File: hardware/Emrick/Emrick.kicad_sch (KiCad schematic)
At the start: 86 parts, among them J1 LED_STRIP_CONNECTOR, J3 Conn_02x05_Odd_Even, J4 BATT_CONN, P1 USB_C_Plug_USB2.0, Q1 Q_NMOS_GSD, Q2 Q_NMOS_GSD, Q3 Q_NMOS_GSD, SW1 SW_SPST, U1 74HCT541, U2 CC1310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

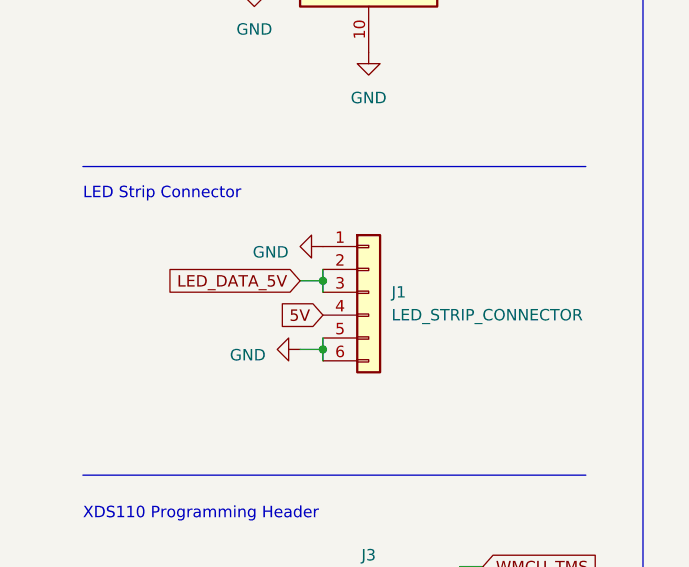
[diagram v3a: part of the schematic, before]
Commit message: update bom and change to horizontal PA connector footprint
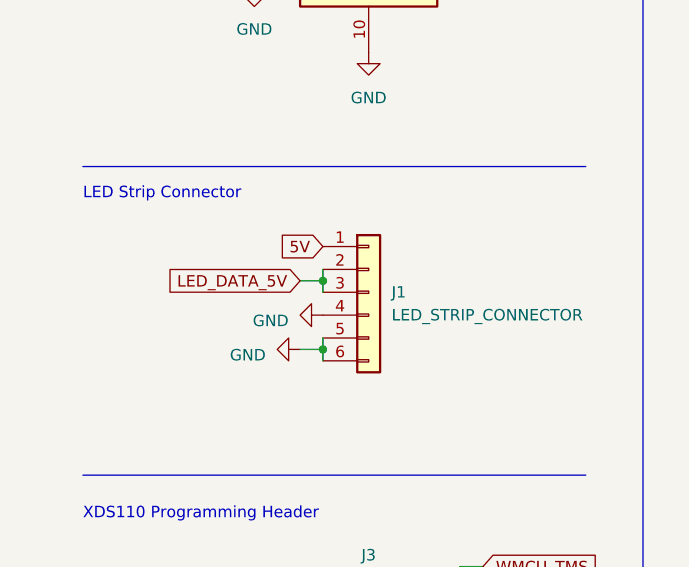
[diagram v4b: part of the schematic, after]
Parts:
- J1: footprint jstpa:CONN-SMD_BM04B-PASS-1-TFT -> jstpa:CONN-SMD_SM04B-PASS-TBT-LF-SN
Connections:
- net 5V: now also J1.1 (Pin_1); no longer J1.4 (Pin_4)
- net GND: now also J1.4 (Pin_4); no longer J1.1 (Pin_1)
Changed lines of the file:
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@@
     (title "Project Emrick Light Strip")
     (date "2022-10-10")
-    (rev "4")
+    (rev "4.1")
   )
   (junction (at 36.83 43.18) (diameter 0) (color 0 0 0 0)
@@
     )
   )
-  (global_label "5V" (shape input) (at 44.45 97.79 180) (fields_autoplaced)
+  (global_label "5V" (shape input) (at 44.45 90.17 180) (fields_autoplaced)
     (effects (font (size 1.27 1.27)) (justify right))
-    (property "Intersheetrefs" "${INTERSHEET_REFS}" (at 32.7236 97.7106 0)
+    (property "Intersheetrefs" "${INTERSHEET_REFS}" (at 32.7236 90.0906 0)
       (effects (font (size 1.27 1.27)) (justify right) hide)
     )
@@
     )
   )
-  (symbol (lib_id "power:GND") (at 44.45 90.17 270) (unit 1)
+  (symbol (lib_id "power:GND") (at 44.45 97.79 270) (unit 1)
     (in_bom yes) (on_board yes) (dnp no) (fields_autoplaced)
-    (property "Reference" "#PWR012" (at 38.1 90.17 0)
+    (property "Reference" "#PWR012" (at 38.1 97.79 0)
       (effects (font (size 1.27 1.27)) hide)
     )
-    (property "Value" "GND" (at 40.64 90.805 90)
+    (property "Value" "GND" (at 40.64 98.425 90)
       (effects (font (size 1.27 1.27)) (justify right))
     )
-    (property "Footprint" "" (at 44.45 90.17 0)
+    (property "Footprint" "" (at 44.45 97.79 0)
       (effects (font (size 1.27 1.27)) hide)
     )
-    (property "Datasheet" "" (at 44.45 90.17 0)
+    (property "Datasheet" "" (at 44.45 97.79 0)
       (effects (font (size 1.27 1.27)) hide)
     )
@@
       (effects (font (size 1.27 1.27)) (justify left))
     )
-    (property "Footprint" "jstpa:CONN-SMD_BM04B-PASS-1-TFT" (at 49.53 95.25 0)
+    (property "Footprint" "jstpa:CONN-SMD_SM04B-PASS-TBT-LF-SN" (at 49.53 95.25 0)
       (effects (font (size 1.27 1.27)) hide)
     )

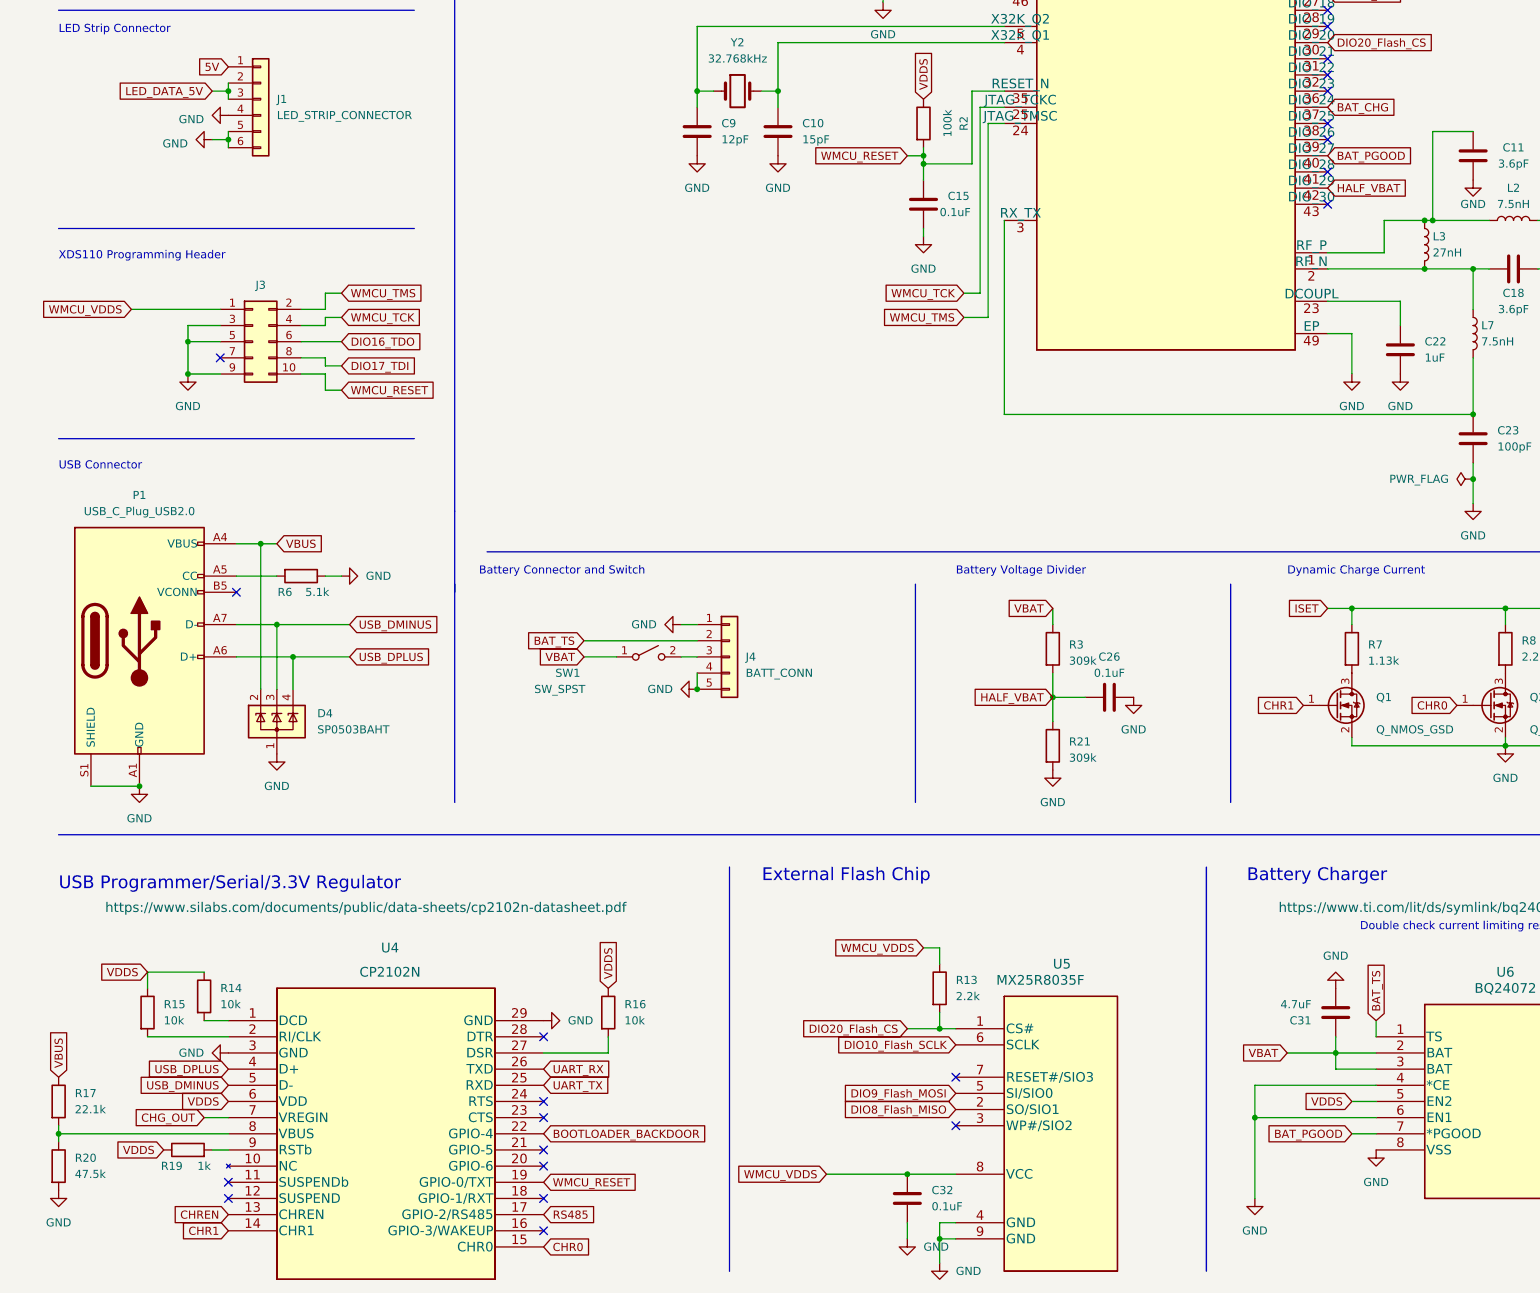
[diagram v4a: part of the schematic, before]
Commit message: Hardware modifications for rev 5
- Added control for battery charging to the microcontroller by connecting
CHARGE_ENABLE, BAT_EN1, and BAT_EN2 to pins on the micro.
- Modified the USB connector and schematic to support bidirectional USB insertion.
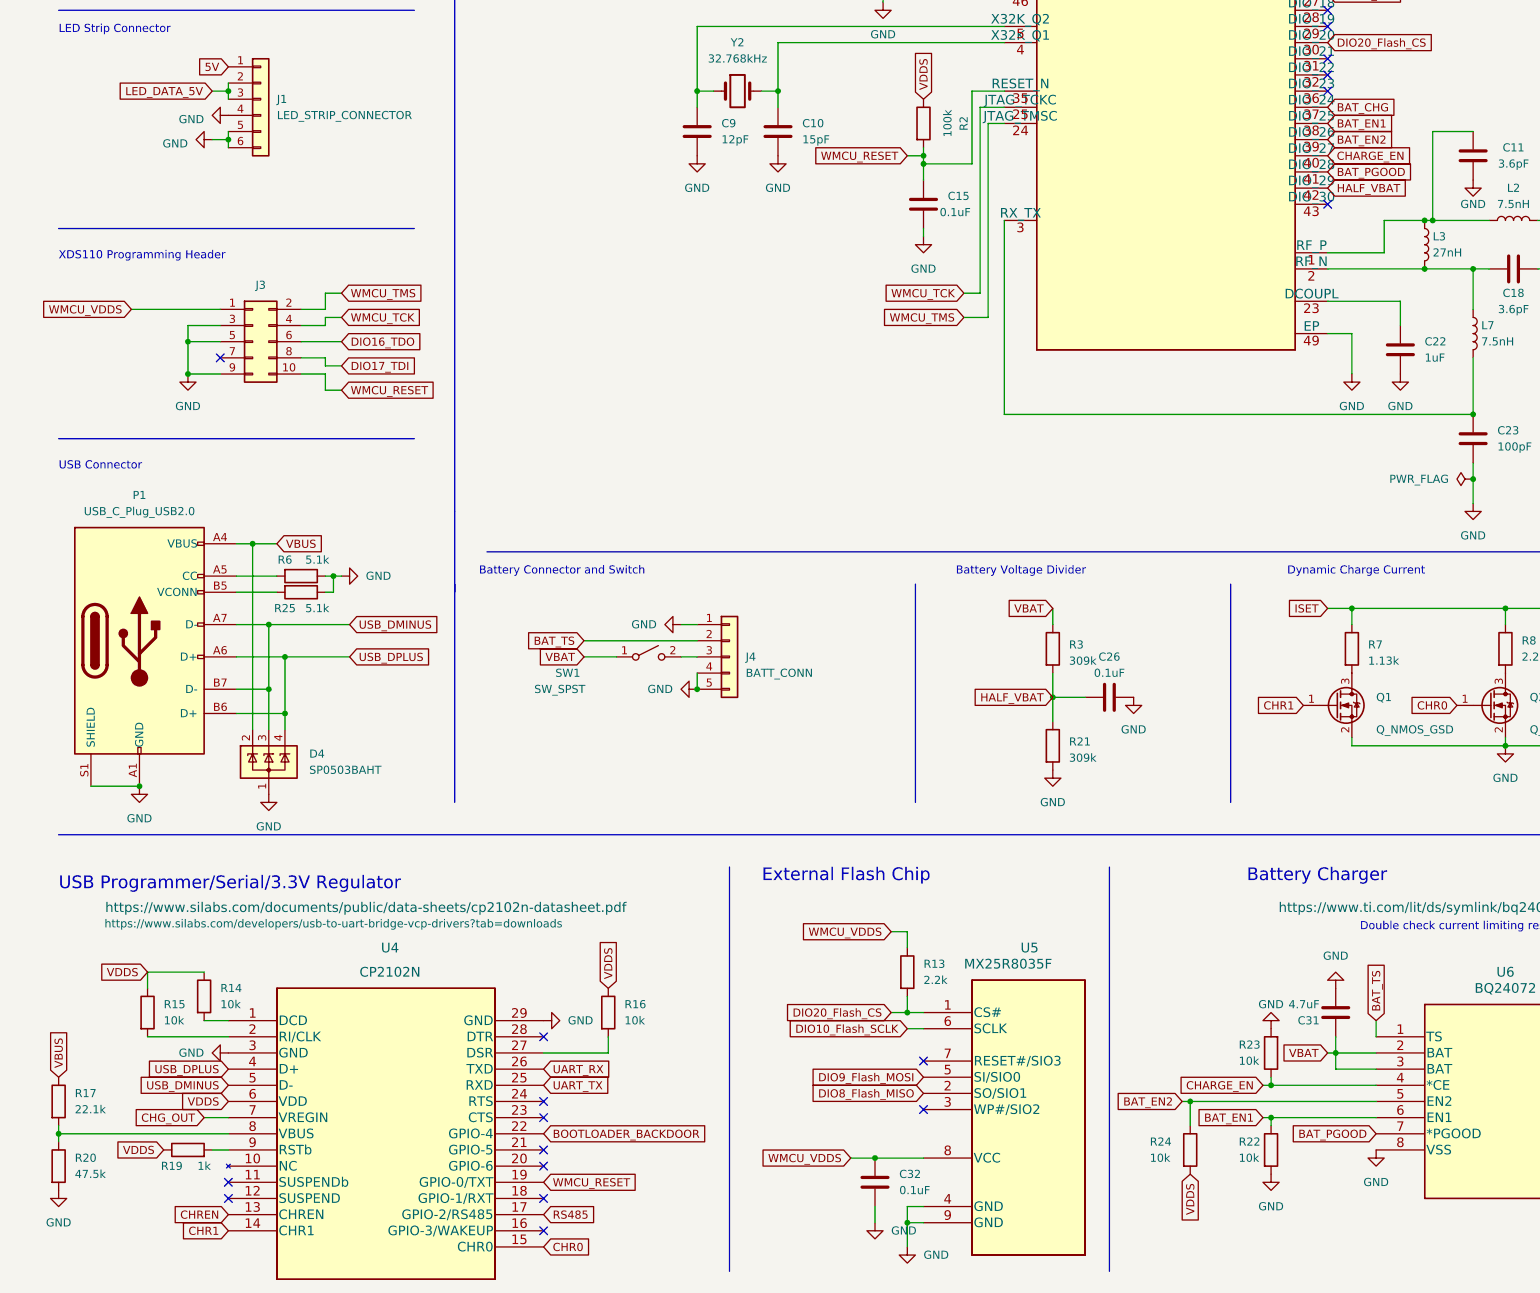
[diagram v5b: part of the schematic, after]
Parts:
- added R22, R23, R24: 10k, Resistor_SMD:R_0402_1005Metric, symbol Device:R
- added R25: 5.1k, Resistor_SMD:R_0402_1005Metric, symbol Device:R
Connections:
- net BAT_PGOOD: now also U2.41 (DIO_28); no longer U2.40 (DIO_27)
- net GND: now also R22.2, R23.2, R25.1; no longer U6.4 (*CE), U6.6 (EN1)
- net USB_DMINUS: now also P1.B7 (D-)
- net USB_DPLUS: now also P1.B6 (D+)
- net VDDS: now also R24.2; no longer U6.5 (EN2)
- net BAT_EN1: now reaches U2.38 (DIO_25)
- net BAT_EN1: now also U6.6 (EN1), R22.1
- net BAT_EN2: now reaches U2.39 (DIO_26)
- net BAT_EN2: now also U6.5 (EN2), R24.1
- net at P1.B5 (VCONN): now also R25.2
- new net CHARGE_EN: R23.1, U2.40 (DIO_27), U6.4 (*CE)
- no-connect marks 34 -> 30
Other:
- moved on the sheet: C32, D4, R13, U5
